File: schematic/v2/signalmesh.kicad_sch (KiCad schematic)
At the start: 15 parts, among them U27 MCP2551-I-P, U29 MCP2551-I-P, U30 MCP2551-I-P, U31 MCP2551-I-P

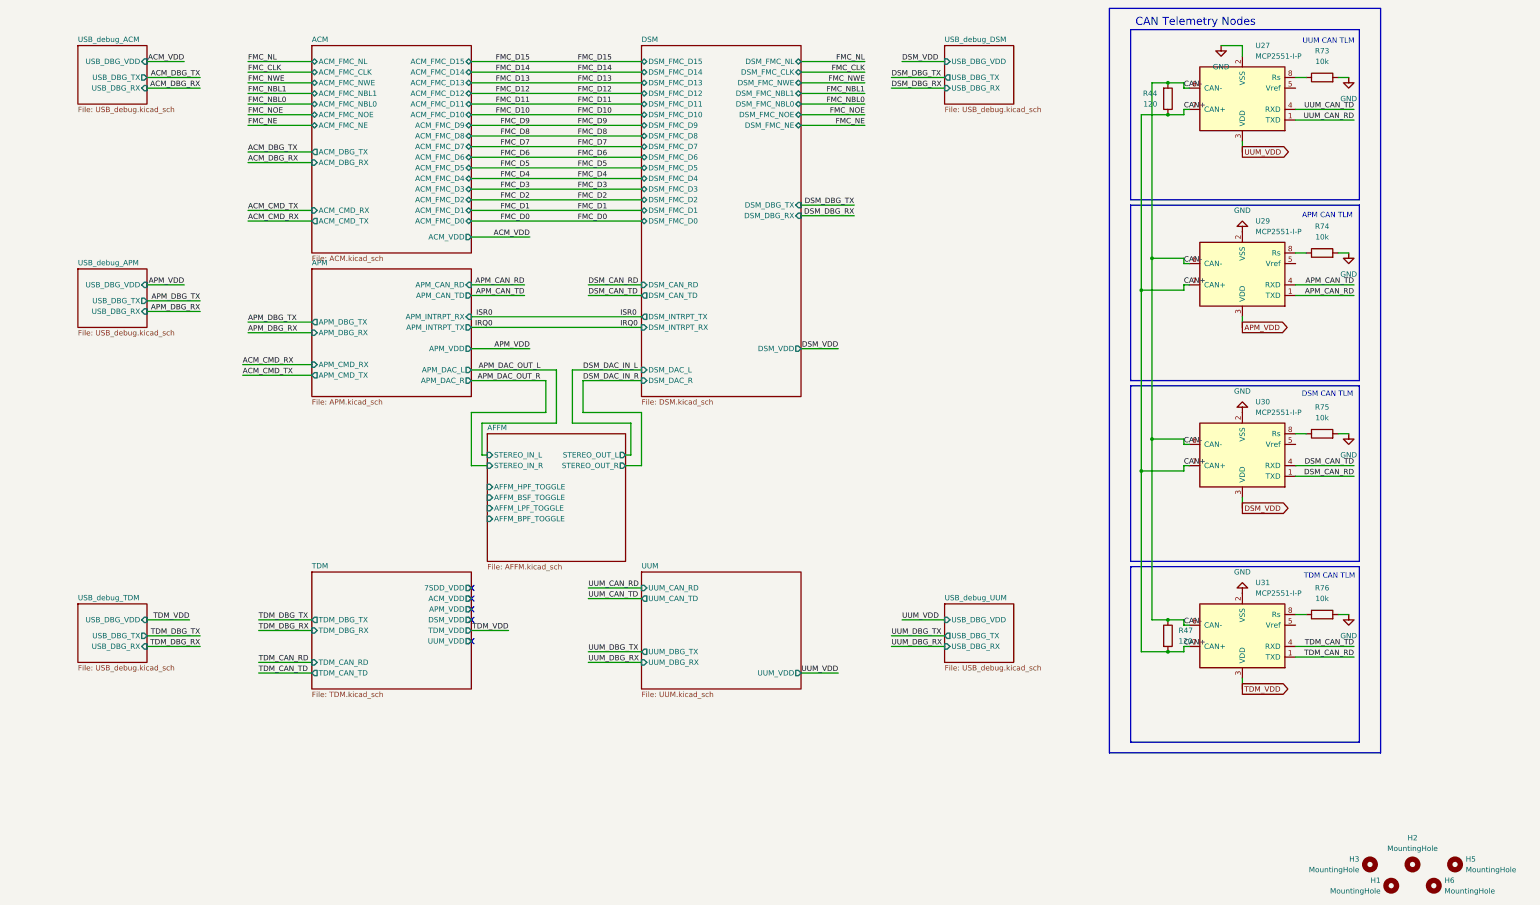
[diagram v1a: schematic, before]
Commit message: now making a v3 with HATs for each nucleo with my needed shit. this will make things very compact and hopefully much cheaper
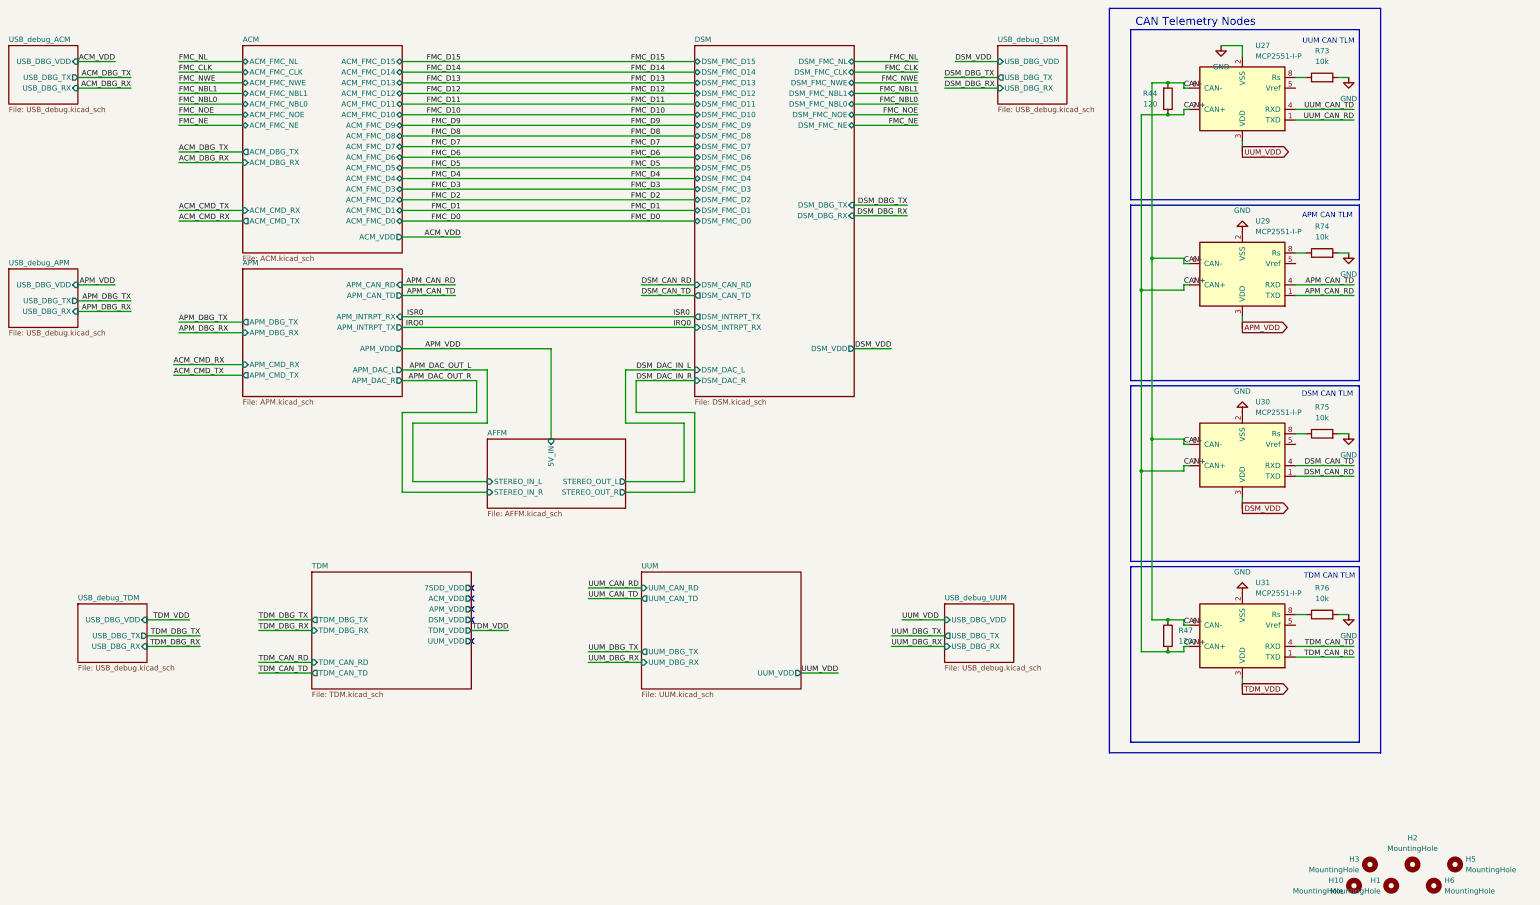
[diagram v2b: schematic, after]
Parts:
- added H10: MountingHole, MountingHole:MountingHole_3.2mm_M3, symbol Mechanical:MountingHole
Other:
- sheet AFFM ports: added 5V_IN; removed AFFM_BPF_TOGGLE, AFFM_BSF_TOGGLE, AFFM_HPF_TOGGLE, AFFM_LPF_TOGGLE
